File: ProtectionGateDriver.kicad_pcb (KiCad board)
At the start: 2 copper layers, 19 parts, among them J1 48V_INPUT_XT_MALE, J2 WHEEL_OUTPUT_XT_FEMALE, J3 12V_GATE_SUPPLY, J4 STM_CONTROL, Q1 MCTL1D0N08Y, U1 1EDN7550B

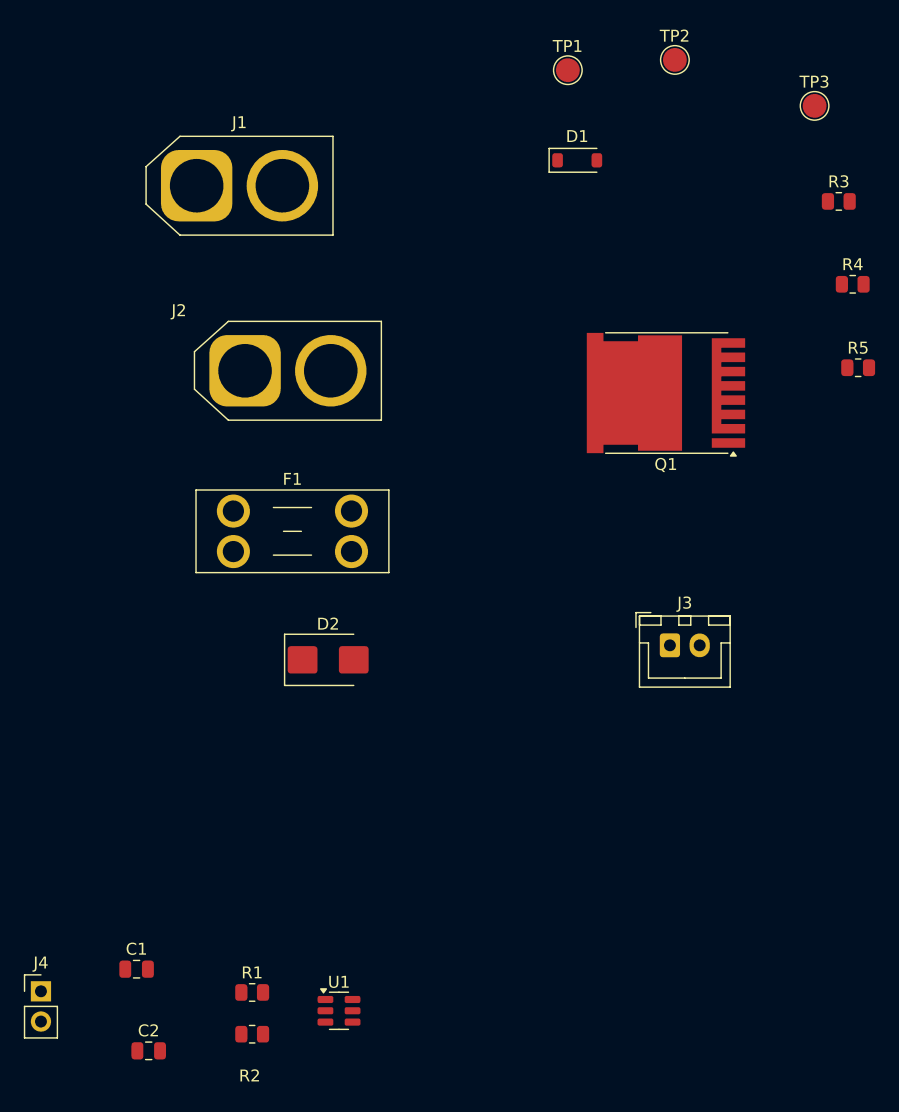
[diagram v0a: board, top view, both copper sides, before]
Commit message: Save first PCB layout iteration — not for fabrication
Upload current KiCad layout and project settings, update schematic and layout previews, and document this as a preliminary review checkpoint. Not a final fabrication version; hardware validation remains outstanding.
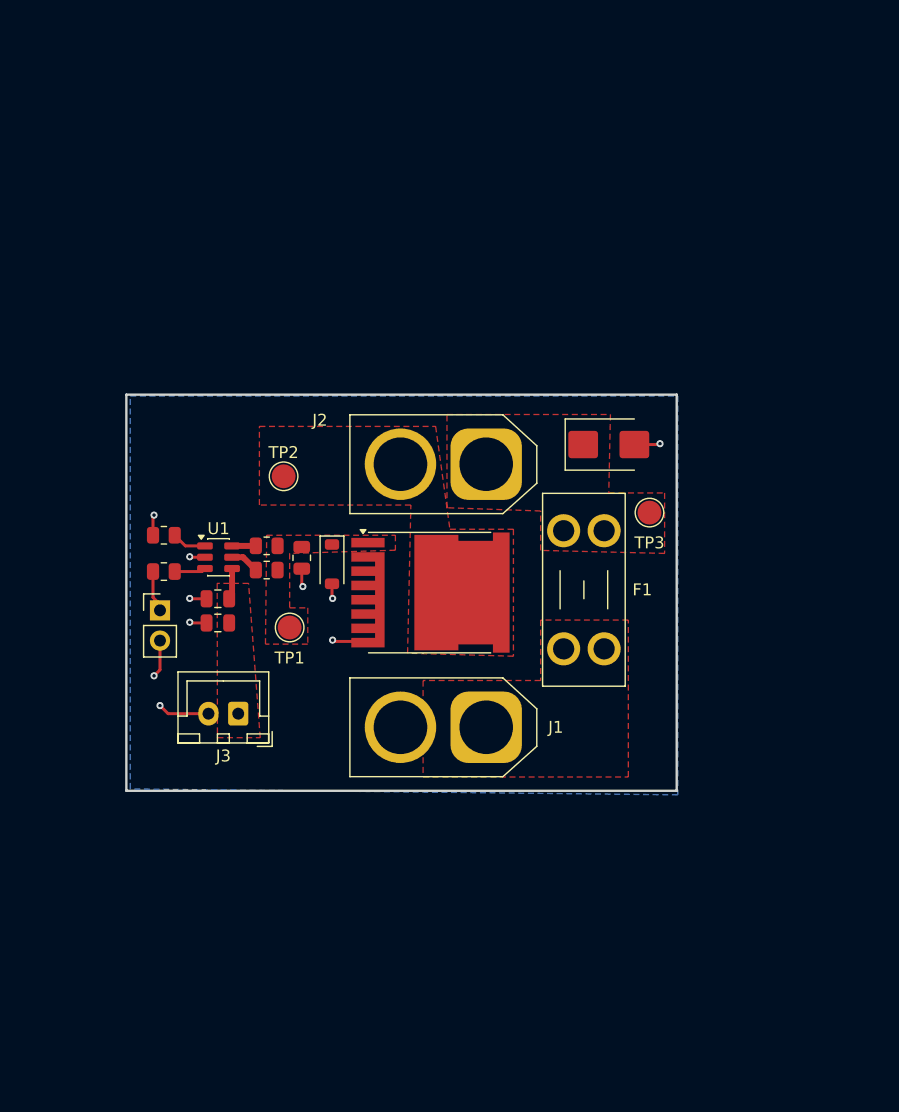
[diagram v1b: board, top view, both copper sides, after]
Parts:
- moved R3 57.2 mm to (134.0, 94.6)
- moved R4 53.9 mm to (134.0, 92.6)
- moved TP1 52.3 mm to (135.9, 99.4)
- moved J1 51.6 mm to (152.4, 107.8), turned to 180 degrees
- moved R5 49.4 mm to (136.9, 93.6), turned to 90 degrees
- moved TP2 48.0 mm to (135.4, 86.7)
- moved R2 42.6 mm to (125.3, 91.7)
- moved D1 39.7 mm to (139.4, 94.1), turned to -90 degrees
- moved U1 39.4 mm to (129.9, 93.5)
- moved TP3 36.9 mm to (166.1, 89.8)
- moved J3 36.7 mm to (131.6, 106.7), turned to 180 degrees
- moved C2 36.4 mm to (129.9, 99.1), turned to 180 degrees
- moved R1 36.1 mm to (125.3, 94.7)
- moved J4 33.5 mm to (125.0, 98.0)
- moved C1 31.9 mm to (129.9, 97.0), turned to 180 degrees
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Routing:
- net GND: track 0.00 -> 22.4 mm, vias 0 -> 10
- net STM32_ENABLE: track 0.00 -> 3.50 mm
- net Net-(U1-IN-): track 0.00 -> 2.91 mm
- net Net-(U1-IN+): track 0.00 -> 2.65 mm
- net +12V: track 0.00 -> 2.64 mm
- net Net-(U1-OUT_SRC): track 0.00 -> 2.44 mm
- net Net-(U1-OUT_SNK): track 0.00 -> 2.00 mm
- added copper zone on F.Cu, net +12V
- added copper zone on F.Cu, net +48V
- added copper zone on F.Cu, net /Q1_GATE
- added copper zone on F.Cu, net /output_neg
- added copper zone on B.Cu, net GND
- added copper zone on F.Cu, net wheel_48V_fused
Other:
- board outline added: 46.2 x 33.3 mm

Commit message: Correct iteration 2 native KiCad files from uploaded project
Replace stale PCB, project and schematic with the supplied iteration 2 files. Four-layer layout is a review checkpoint, not for fabrication.
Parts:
- TP1, TP2, TP3: footprint TestPoint:TestPoint_Pad_D2.0mm -> TestPoint:TestPoint_Pad_D1.0mm
- moved D2 25.4 mm to (161.6, 109.5)
- moved J1 21.8 mm to (152.0, 86.0)
- moved J2 21.5 mm to (152.2, 107.2)
- moved TP2 20.8 mm to (138.8, 107.2)
- moved TP3 16.6 mm to (161.5, 105.8)
- moved TP1 14.2 mm to (138.4, 85.4)
- moved F1 11.9 mm to (162.8, 90.0), turned to -90 degrees
- moved J4 6.48 mm to (129.1, 93.0)
- moved R1 6.10 mm to (129.1, 90.0)
- moved C1 5.95 mm to (133.4, 92.2)
- moved C2 5.95 mm to (133.4, 94.2)
- moved R3 5.90 mm to (137.5, 89.9)
- moved R4 5.90 mm to (137.5, 87.8)
- moved U1 5.90 mm to (133.4, 88.8)
- moved R2 5.51 mm to (129.1, 87.7)
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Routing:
- net GND: track 22.4 -> 6.28 mm, vias 10 -> 22
- net /Q1_GATE: track 0.00 -> 12.5 mm
- net Net-(U1-IN-): track 2.91 -> 2.26 mm
- added copper zone on In2.Cu, net +48V
- added copper zone on F.Cu, net GND
- added copper zone on In1.Cu, net GND
- removed copper zone on F.Cu, net +48V
- removed copper zone on F.Cu, net /Q1_GATE
- removed copper zone on B.Cu, net GND
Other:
- board size 46.2 x 33.3 mm -> 39.6 x 33.6 mm
- copper layers 2 -> 4

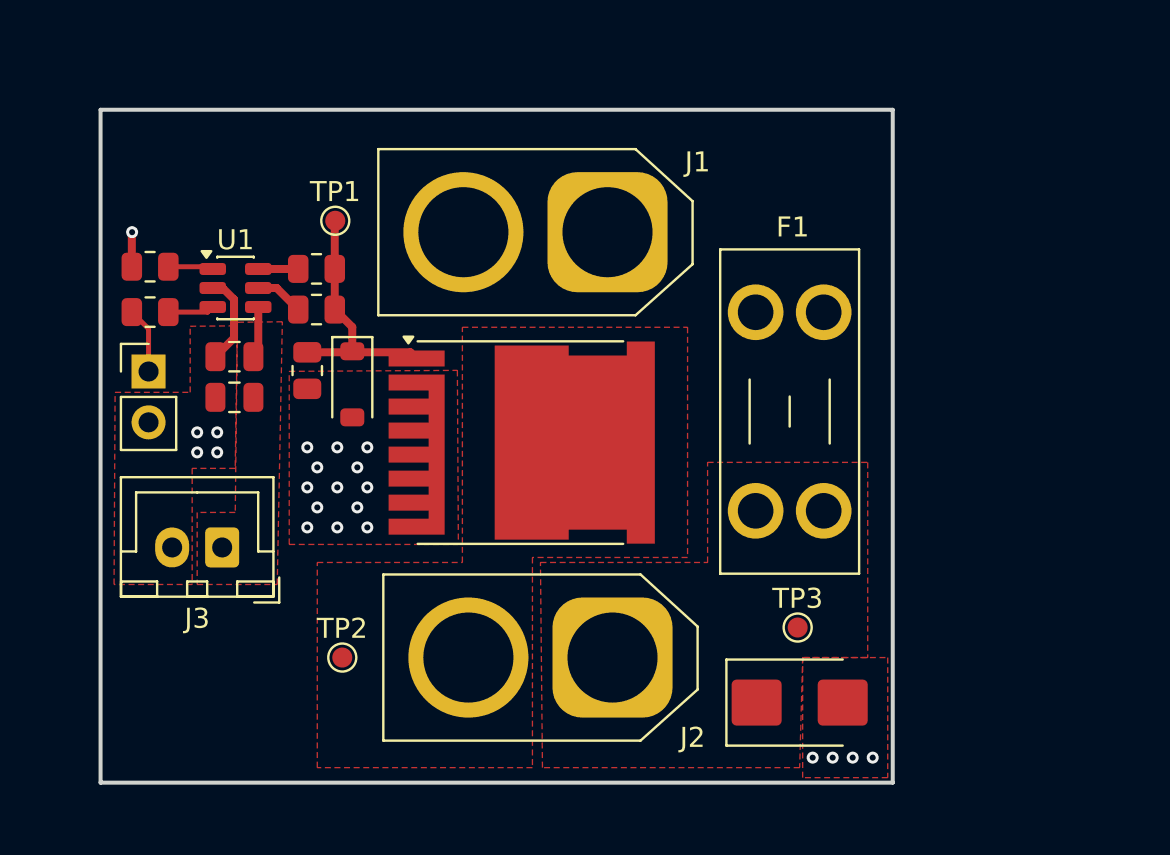
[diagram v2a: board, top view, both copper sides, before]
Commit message: Save third protection-board layout iteration with native KiCad files
Add input capacitor, M2 mounting holes, rounded outline and updated screenshots. Development checkpoint only; not for fabrication.
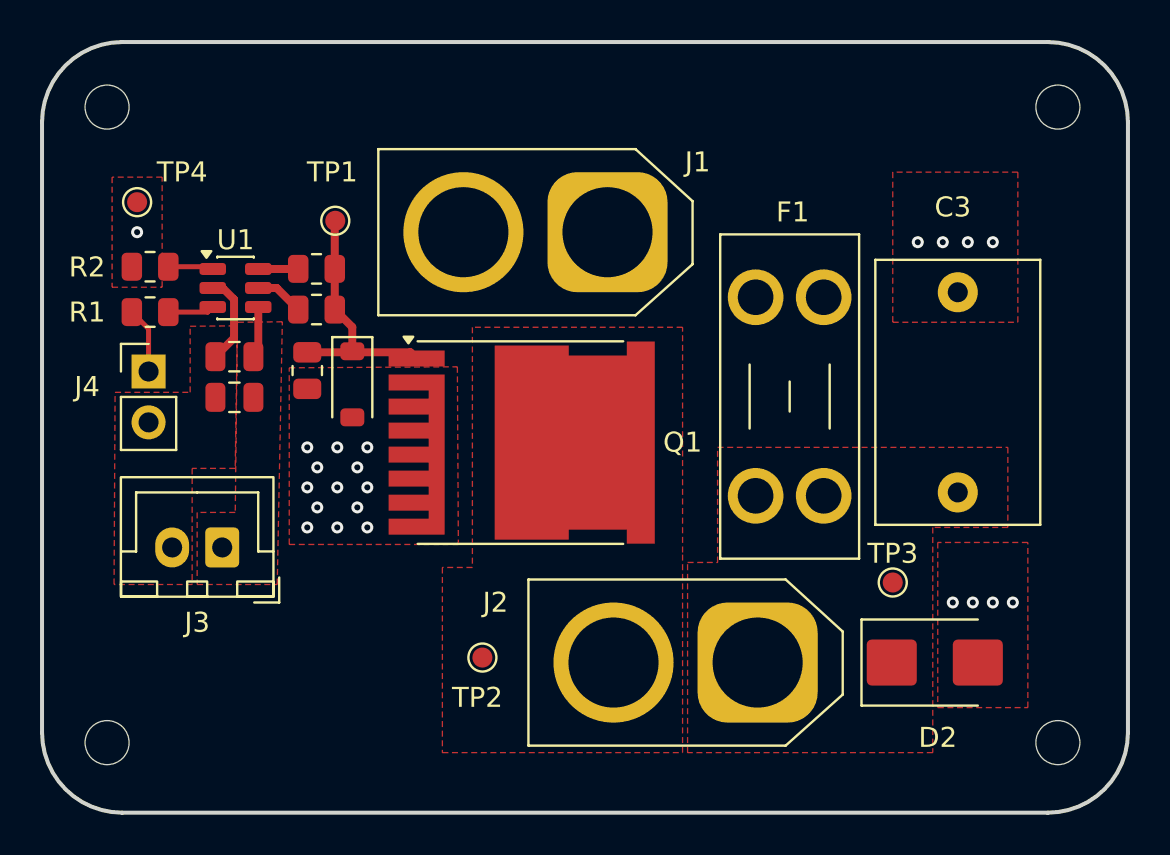
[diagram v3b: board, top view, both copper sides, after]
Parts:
- added C3: 1uF, Capacitor_THT:C_Rect_L13.0mm_W8.0mm_P10.00mm_FKS3_FKP3_MKS4, F.Cu at (169.5, 99.0)
- added H1: MountingHole, MountingHole:MountingHole_2.2mm_M2, F.Cu at (127.0, 79.8)
- added H2: MountingHole, MountingHole:MountingHole_2.2mm_M2, F.Cu at (174.5, 79.8)
- added H3: MountingHole, MountingHole:MountingHole_2.2mm_M2, F.Cu at (174.5, 111.5)
- added H4: MountingHole, MountingHole:MountingHole_2.2mm_M2, F.Cu at (127.0, 111.5)
- added TP4: TestPoint, TestPoint:TestPoint_Pad_D1.0mm, F.Cu at (128.5, 84.5)
- moved J2 7.25 mm to (159.5, 107.5)
- moved D2 7.04 mm to (168.3, 107.5)
- moved TP2 7.00 mm to (145.8, 107.2)
- moved TP3 5.26 mm to (166.2, 103.5)
- moved F1 0.75 mm to (162.8, 89.2)
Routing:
- net GND: track 6.28 -> 4.55 mm
- added copper zone on In2.Cu, net wheel_48V_fused
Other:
- board size 39.6 x 33.6 mm -> 54.2 x 38.5 mm
